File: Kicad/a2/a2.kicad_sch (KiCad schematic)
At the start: 60 parts, among them J1 Barrel Jack, J2 IDC 34, J3 Conn_02x03_Odd_Even, J4 VGA, J5 AudioJack4, SW1 SW_Push, SW2 SW_SPDT, U1 74HC590A, U10 74HC32, U11 74HC4520, U12 74HC174, U13 MCP100H, U2 74HC590A, U3 SST39SF0x0, U4 62256, U5 W65C02SxP, U6 74HCT540, U7 74HC166, U8 74HCT04, U9 74HC10, Y1 16Mhz

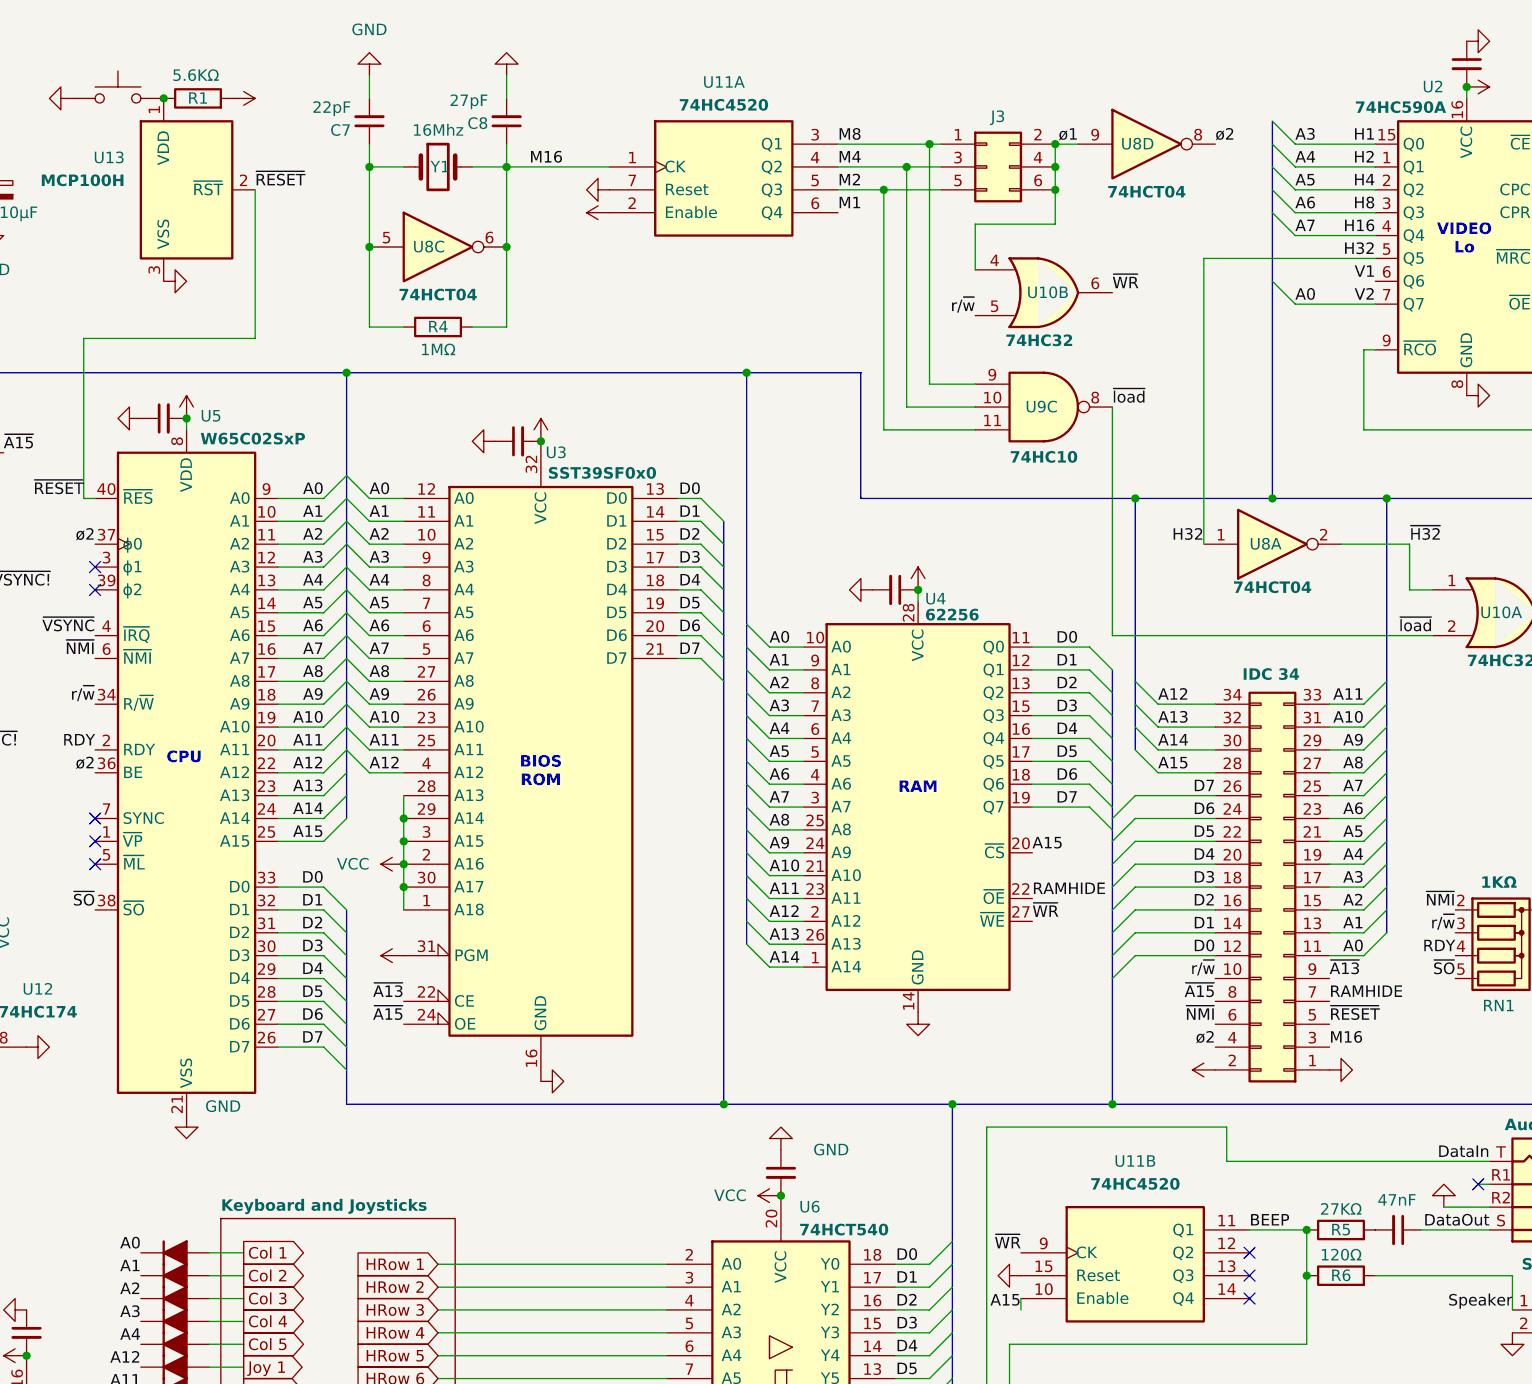
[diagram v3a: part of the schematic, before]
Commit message: tweak resitor values
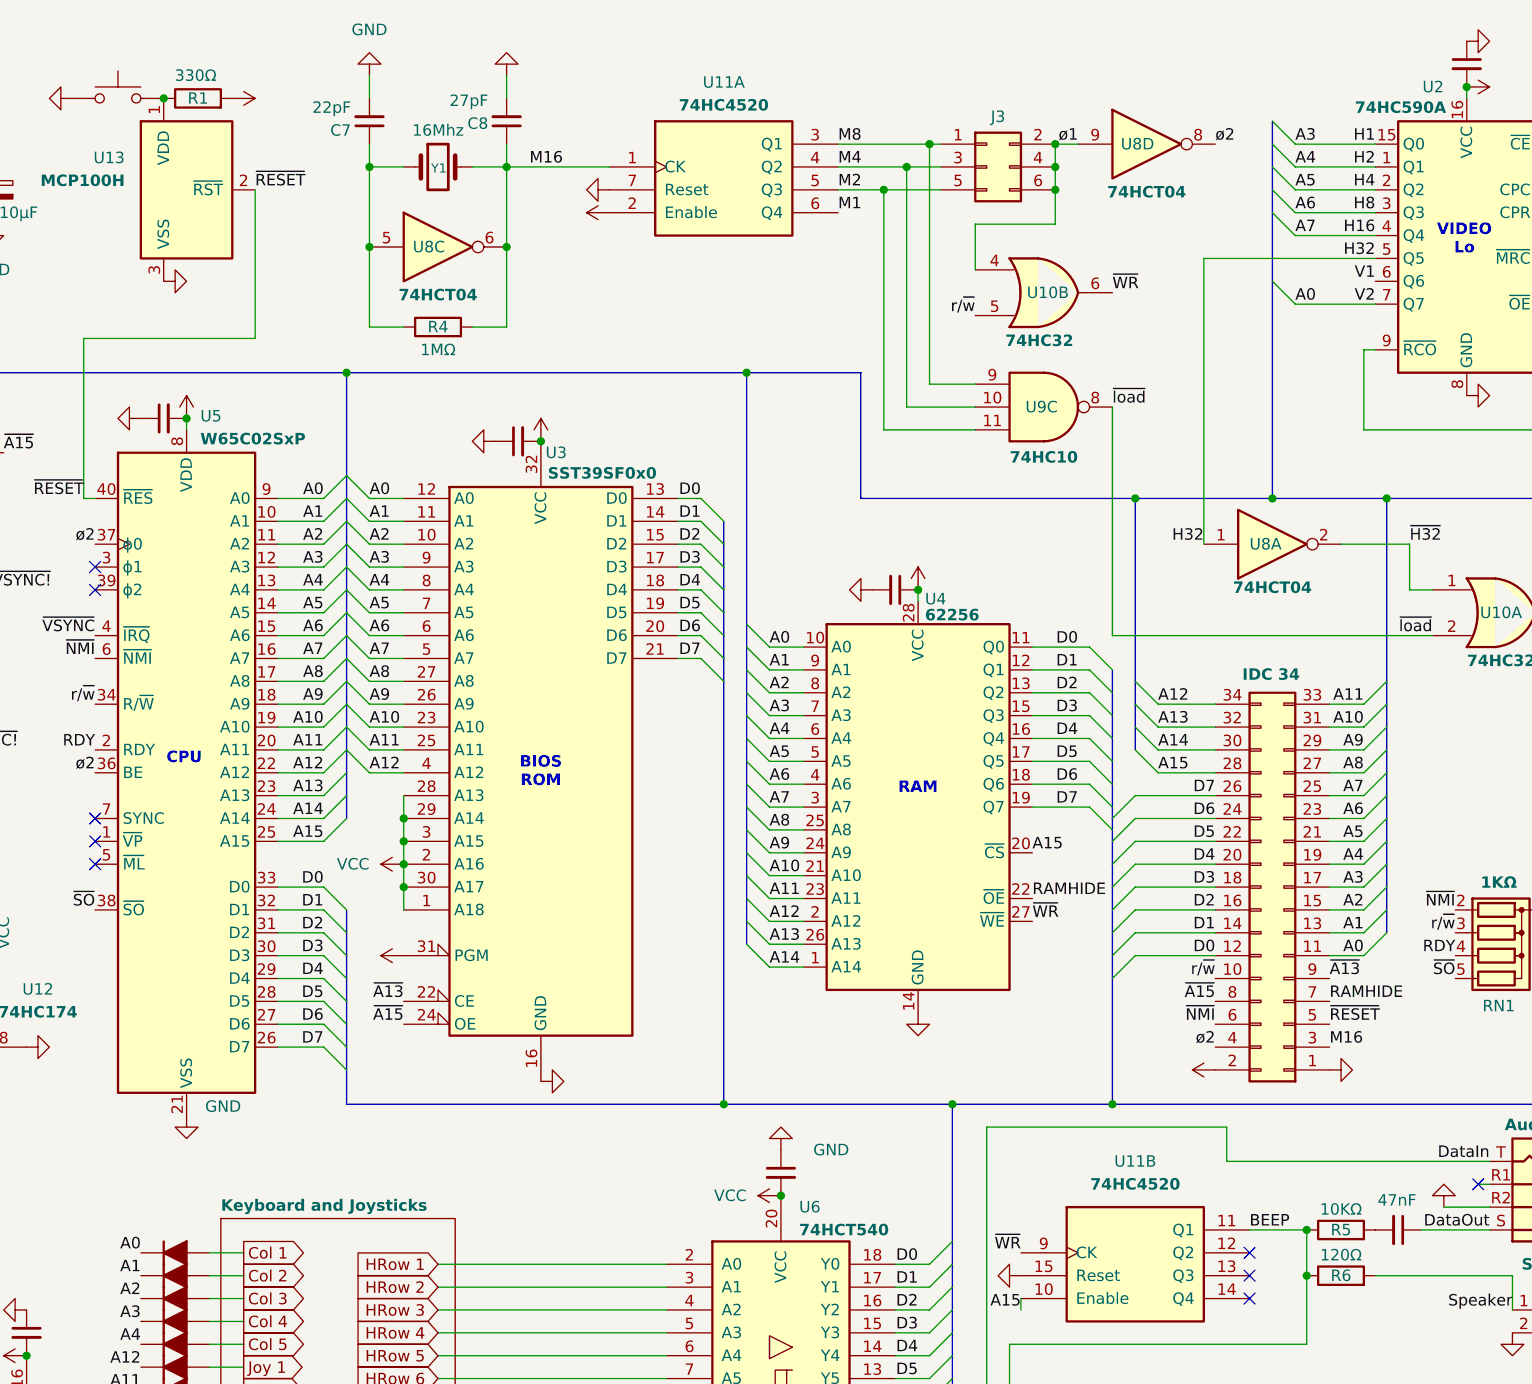
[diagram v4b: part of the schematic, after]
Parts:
- R1: value 5.6KΩ -> 330Ω
- R5: value 27KΩ -> 10KΩ
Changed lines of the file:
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@@
 			)
 		)
-		(property "Value" "27KΩ"
+		(property "Value" "10KΩ"
 			(at 210.82 146.304 90)
 			(effects
@@
 			)
 		)
-		(property "Value" "5.6KΩ"
+		(property "Value" "330Ω"
 			(at 83.566 20.32 90)
 			(effects
@@
 		(dnp no)
 		(property "Reference" "Y1"
-			(at 110.744 30.48 0)
-			(effects
-				(font
-					(size 1.27 1.27)
-				)
-			)
+			(at 110.5896 30.6326 0)
+			(effects
+				(font
+					(size 1.016 1.016)
+				)
+			)
